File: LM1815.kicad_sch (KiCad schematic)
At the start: 13 parts, among them IC2 LM1815MX_NOPB

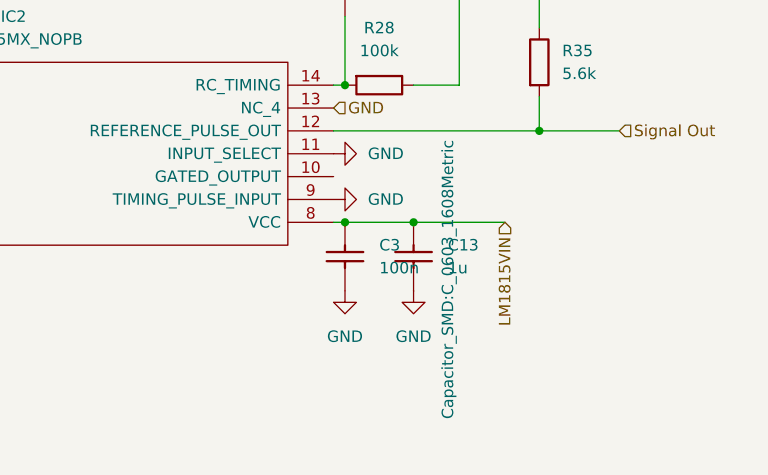
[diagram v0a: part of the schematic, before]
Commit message: Changed component sizes, added stitching vias
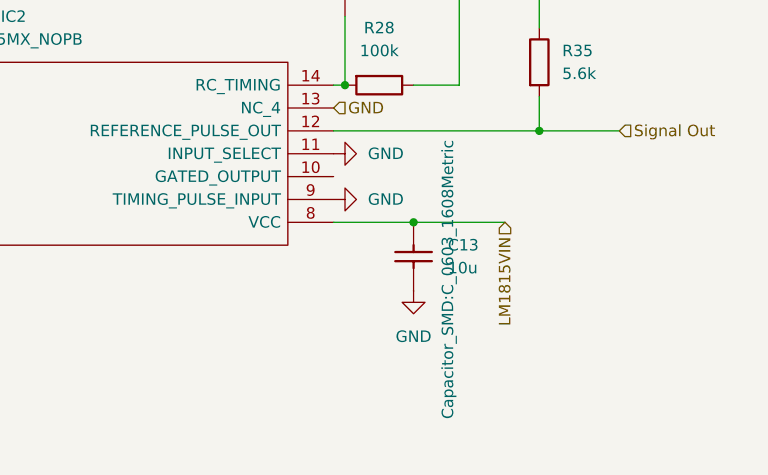
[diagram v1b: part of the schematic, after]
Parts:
- removed C3: 100n, Capacitor_SMD:C_0402_1005Metric, symbol hellen-one-common:Cap
- C13: value 1u -> 10u; LCSC (none) -> C96446; PN (none) -> CL10A106MA8NRNC
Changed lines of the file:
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@@
-	)
-	(junction
-		(at 148.59 69.85)
-		(diameter 0)
-		(color 0 0 0 0)
 	)
 	(junction
@@
 	(wire
 		(pts
-			(xy 156.21 69.85) (xy 148.59 69.85)
+			(xy 147.32 69.85) (xy 156.21 69.85)
 		)
 		(stroke
@@
 		(pts
 			(xy 33.02 59.69) (xy 35.56 59.69)
-		)
-		(stroke
-			(width 0)
-			(type default)
-		)
-	)
-	(wire
-		(pts
-			(xy 148.59 69.85) (xy 147.32 69.85)
 		)
 		(stroke
@@
 	)
 	(symbol
-		(lib_id "power:GND")
-		(at 148.59 77.47 0)
-		(unit 1)
-		(exclude_from_sim no)
-		(in_bom yes)
-		(on_board yes)
-		(dnp no)
-		(fields_autoplaced yes)
-		(property "Reference" "#PWR0101"
-			(at 148.59 83.82 0)
-			(effects
-				(font
-					(size 1.27 1.27)
-				)
-				(hide yes)
-			)
-		)
-		(property "Value" "GND"
-			(at 148.59 82.55 0)
-			(effects
-				(font
-					(size 1.27 1.27)
-				)
-			)
-		)
-		(property "Footprint" ""
-			(at 148.59 77.47 0)
-			(effects
-				(font
-					(size 1.27 1.27)
-				)
-				(hide yes)
-			)
-		)
-		(property "Datasheet" ""
-			(at 148.59 77.47 0)
-			(effects
-				(font
-					(size 1.27 1.27)
-				)
-				(hide yes)
-			)
-		)
-		(property "Description" "Power symbol creates a global label with name \"GND\" , ground"
-			(at 148.59 77.47 0)
-			(effects
-				(font
-					(size 1.27 1.27)
-				)
-				(hide yes)
-			)
-		)
-		(pin "1"
-		)
-		(instances
-			(project ""
-				(path "/90b72e19-92bc-40db-bd4d-f17fb5de93ea/cd060a6c-d287-4cb9-8915-021006085e75"
-					(reference "#PWR0101")
-					(unit 1)
-				)
-			)
-		)
-	)
-	(symbol
 		(lib_id "Device:R")
 		(at 64.77 77.47 0)
@@
 	(symbol
 		(lib_id "hellen-one-common:Cap")
-		(at 148.59 73.66 90)
-		(unit 1)
-		(exclude_from_sim no)
-		(in_bom yes)
-		(on_board yes)
-		(dnp no)
-		(fields_autoplaced yes)
-		(property "Reference" "C3"
-			(at 152.4 72.3899 90)
-			(effects
-				(font
-					(size 1.27 1.27)
-				)
-				(justify right)
-			)
-		)
-		(property "Value" "100n"
-			(at 152.4 74.9299 90)
-			(effects
-				(font
-					(size 1.27 1.27)
-				)
-				(justify right)
-			)
-		)
-		(property "Footprint" "Capacitor_SMD:C_0402_1005Metric"
-			(at 152.4 76.2 0)
-			(effects
-				(font
-					(size 1.27 1.27)
-				)
-				(hide yes)
-			)
-		)
-		(property "Datasheet" ""
-			(at 148.59 77.47 90)
-			(effects
-				(font
-					(size 1.27 1.27)
-				)
-				(hide yes)
-			)
-		)
-		(property "Description" "Capacitor"
-			(at 148.59 73.66 0)
-			(effects
-				(font
-					(size 1.27 1.27)
-				)
-				(hide yes)
-			)
-		)
-		(property "LCSC" ""
-			(at 148.59 73.66 0)
-			(effects
-				(font
-					(size 1.27 1.27)
-				)
-				(hide yes)
-			)
-		)
-		(pin "2"
-		)
-		(pin "1"
-		)
-		(instances
-			(project "VFRECU-VR"
-				(path "/90b72e19-92bc-40db-bd4d-f17fb5de93ea/cd060a6c-d287-4cb9-8915-021006085e75"
-					(reference "C3")
-					(unit 1)
-				)
-			)
-		)
-	)
-	(symbol
-		(lib_id "hellen-one-common:Cap")
 		(at 148.59 43.18 90)
 		(unit 1)
@@
 			)
 		)
-		(property "Value" "1u"
+		(property "Value" "10u"
 			(at 160.02 74.9299 90)
 			(effects
@@
 			)
 		)
-		(property "LCSC" ""
+		(property "LCSC" "C96446"
 			(at 156.21 73.66 0)
 			(effects
 				(font
+					(size 1.27 1.27)
+				)
+				(hide yes)
+			)
+		)
+		(property "PN" "CL10A106MA8NRNC"
+			(at 156.21 73.66 90)
+			(effects
+				(font
